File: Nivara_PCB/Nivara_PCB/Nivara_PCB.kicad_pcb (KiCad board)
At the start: 4 copper layers, 120 x 79.5 mm, 183 parts, among them J1 Conn_02x02_Counter_Clockwise, J10 Bolnera 2P, J11 Bolnera 2P, J12 Bolnera 4P, J13 Bolnera 2P, J14 Bolnera 6P, J15 PINHD_2x2_Male, J2 Auxiliares, J3 Bolnera 2P, J4 Bolnera 3P, J5 Bolnera 2P, J6 Bolnera 2P, J7 Bolnera 2P, J8 Bolnera 2P, J9 Bolnera 3P, K1 SRA-24VDC-CL, K2 SRA-24VDC-CL, Q1 IRLML0040, Q2 AO3407A, Q3 IRLML0040, Q4 AO3407A, Q5 IRLML6402TRPBF-JSM, SW3 SW_Push, SW4 SW_Push, U1 GT-USB-7010ASV, U10 LTV-357T, U11 LTV-357T, U12 GP8201S-TC50-EW, U13 LK1802, U14 LTV-357T, U15 LTV-357T, U16 LTV-357T, U17 LTV-357T, U18 LTV-357T, U19 LTV-357T, U20 LTV-357T, U21 GP8303-TC50-EW, U5 ESP32-S3-WROOM-1, U6 AP63200WU, U7 RSM3485ECHT_C2992406, U8 LTV-357T, U9 LTV-357T

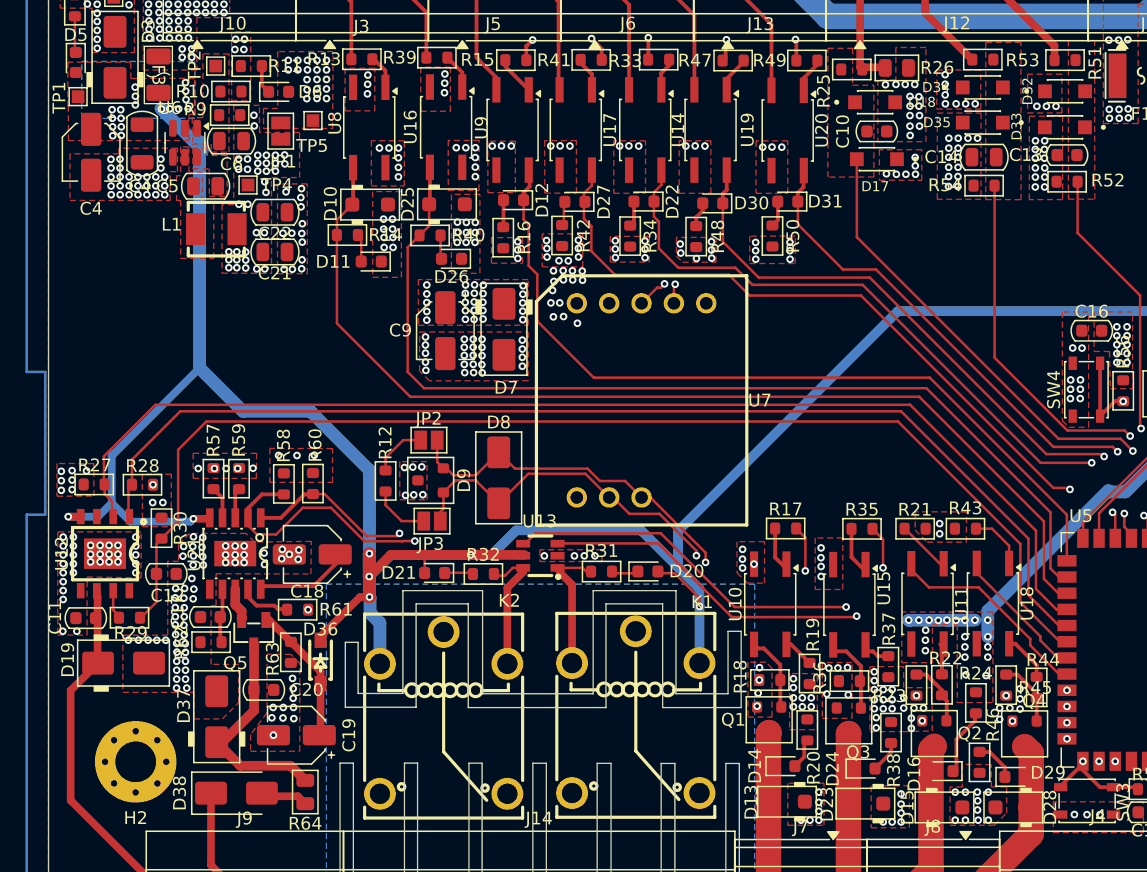
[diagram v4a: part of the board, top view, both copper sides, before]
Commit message: Cambios en las silscreen de los componentes.
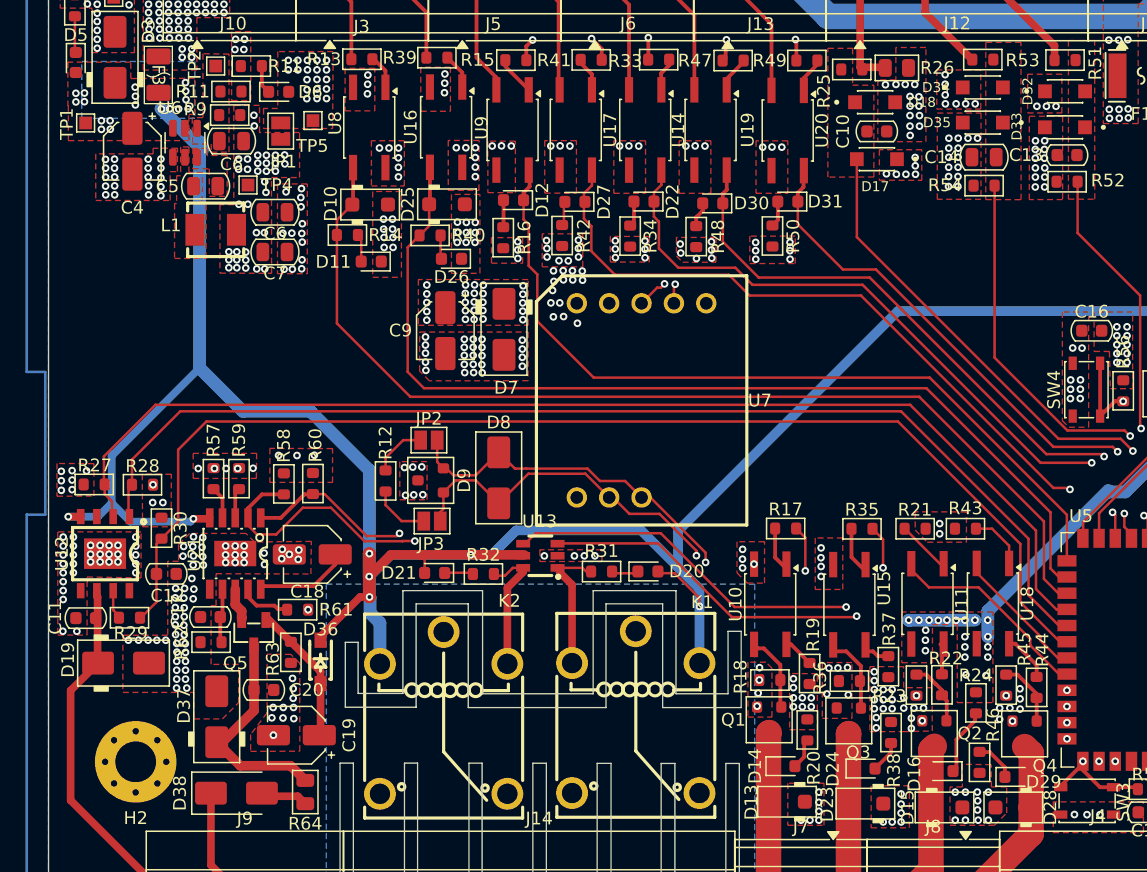
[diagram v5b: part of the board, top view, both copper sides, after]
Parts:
- removed the C4 at (36.8, 36.7)
- moved C4 3.24 mm to (36.0, 37.3)
- moved TP1 2.15 mm to (32.3, 35.1)
- moved L1 0.07 mm to (42.5, 43.5)
- renumbered C22 to C6, C21 to C7, R10 to R11
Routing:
- net GND: vias 321 -> 314
